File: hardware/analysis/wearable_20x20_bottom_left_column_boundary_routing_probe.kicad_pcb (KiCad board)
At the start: 4 copper layers, 49.3 x 49.3 mm, 400 parts

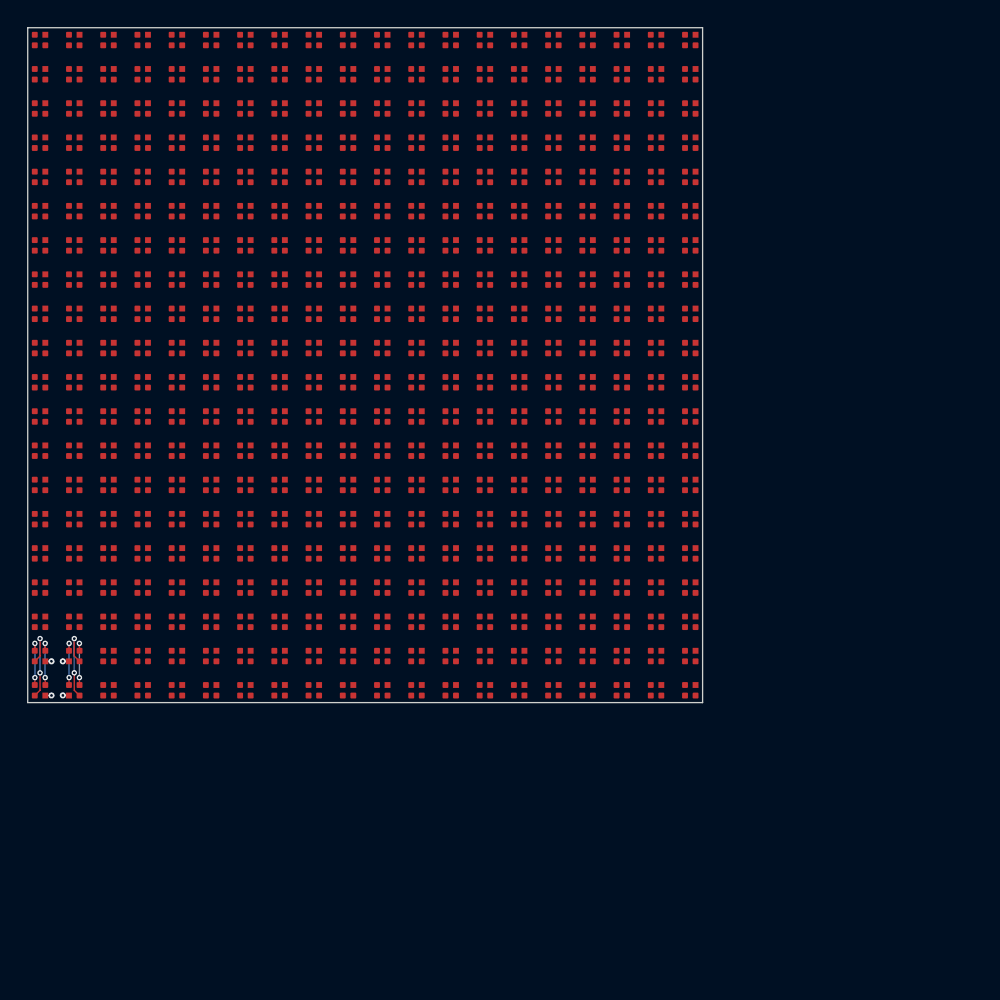
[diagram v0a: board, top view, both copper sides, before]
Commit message: Place 20x20 backside parts outside the via field
Co-authored-by: illiapliukhin <illiapliukhin@users.noreply.github.com>
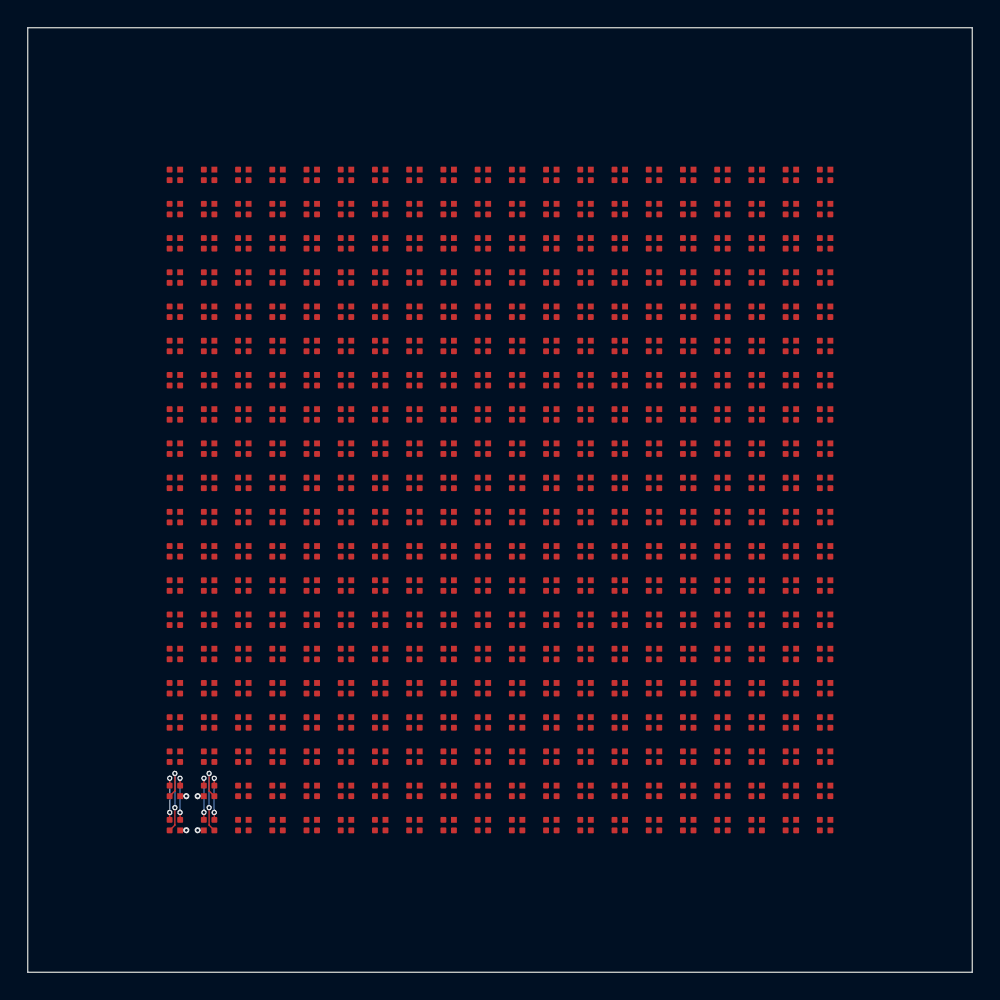
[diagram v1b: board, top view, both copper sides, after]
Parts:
- moved D1 13.9 mm to (10.8, 10.8)
- moved D101 13.9 mm to (10.8, 23.2)
- moved D104 13.9 mm to (18.2, 23.2)
- moved D105 13.9 mm to (20.8, 23.2)
- moved D106 13.9 mm to (23.2, 23.2)
- moved D107 13.9 mm to (25.8, 23.2)
- moved D121 13.9 mm to (10.8, 25.8)
- moved D124 13.9 mm to (18.2, 25.8)
- moved D125 13.9 mm to (20.8, 25.8)
- moved D126 13.9 mm to (23.2, 25.8)
- moved D127 13.9 mm to (25.8, 25.8)
- moved D4 13.9 mm to (18.2, 10.8)
- moved D5 13.9 mm to (20.8, 10.8)
- moved D6 13.9 mm to (23.2, 10.8)
- moved D61 13.9 mm to (10.8, 18.2)
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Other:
- board size 49.3 x 49.3 mm -> 69 x 69 mm
